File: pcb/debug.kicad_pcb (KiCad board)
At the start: 4 copper layers, 50 x 100 mm, 78 parts, among them J1 09032967825, J2 USB_C_Receptacle_USB2.0, J3 Conn_01x06_Female, Q1 Q_PNP_BCE, SW1 SW_DIP_x02, SW2 Reset, U1 STLQ020PU33R, U2 FT4222HQ, U3 STM32F103V8Tx, U4 INA381AxDSG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

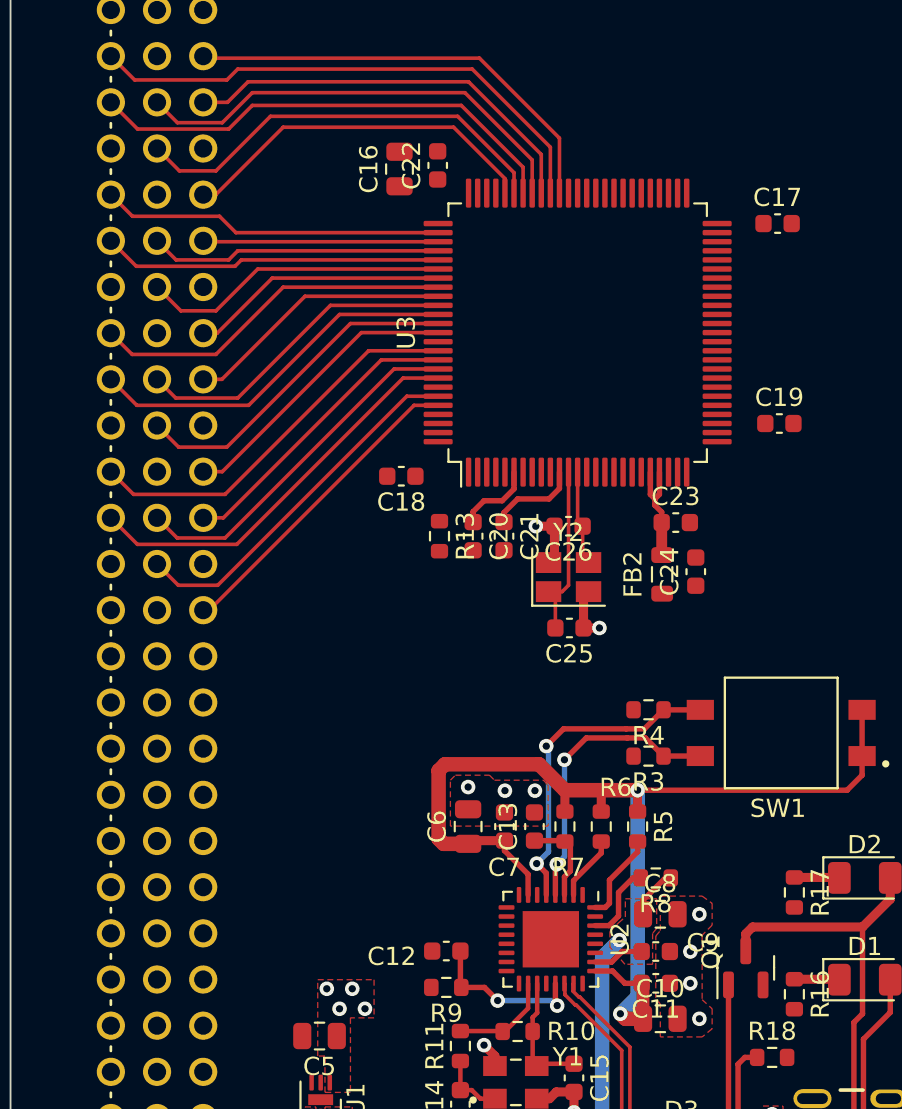
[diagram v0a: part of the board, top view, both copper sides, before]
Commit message: route more data traces
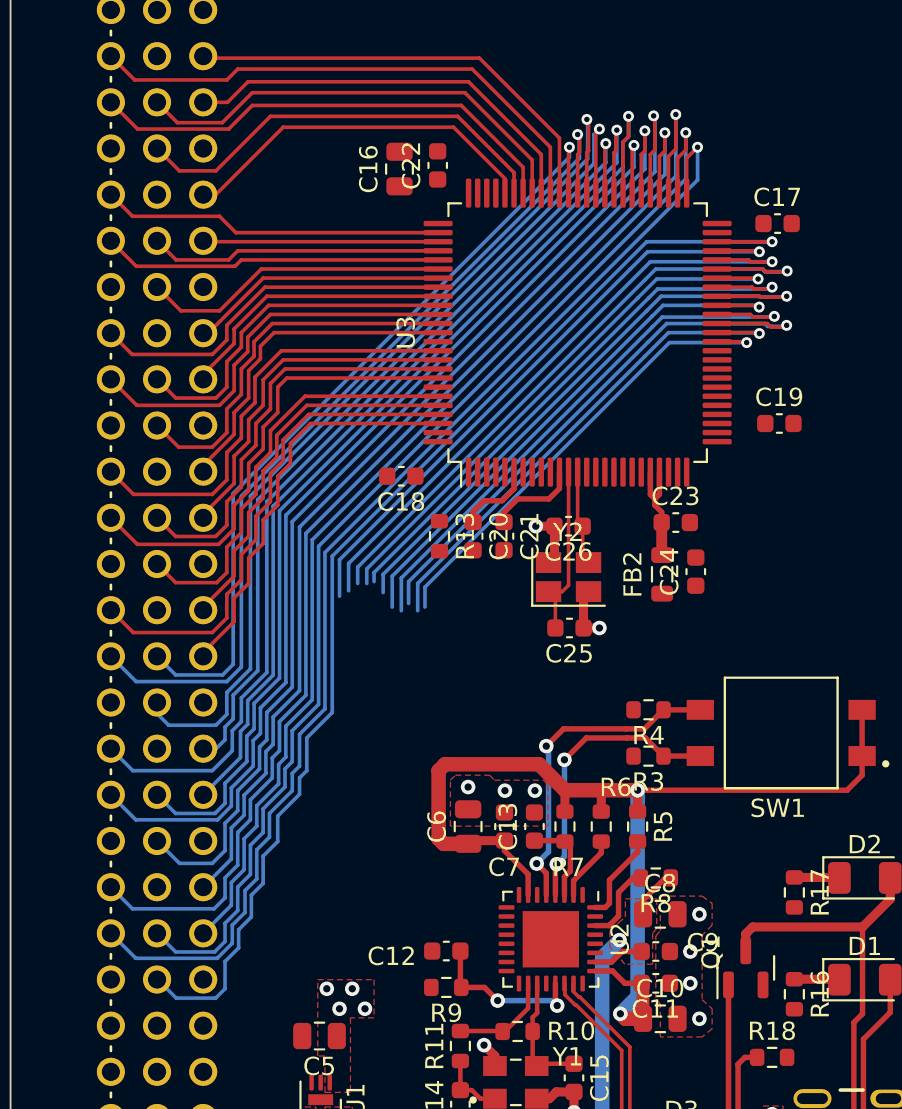
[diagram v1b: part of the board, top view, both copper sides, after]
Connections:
- U3 pad 37: unconnected-(U3-Pad37) -> CONN_0
- U3 pad 38: unconnected-(U3-Pad38) -> CONN_1
- U3 pad 39: unconnected-(U3-Pad39) -> CONN_2
- U3 pad 40: unconnected-(U3-Pad40) -> CONN_3
- U3 pad 41: unconnected-(U3-Pad41) -> CONN_4
- U3 pad 42: unconnected-(U3-Pad42) -> CONN_5
- U3 pad 43: unconnected-(U3-Pad43) -> CONN_6
- U3 pad 44: unconnected-(U3-Pad44) -> CONN_7
- U3 pad 45: unconnected-(U3-Pad45) -> CONN_8
- U3 pad 46: unconnected-(U3-Pad46) -> CONN_9
- U3 pad 47: unconnected-(U3-Pad47) -> CONN_10
- U3 pad 48: unconnected-(U3-Pad48) -> CONN_11
- U3 pad 51: unconnected-(U3-Pad51) -> CONN_12
- U3 pad 52: unconnected-(U3-Pad52) -> CONN_13
- U3 pad 53: unconnected-(U3-Pad53) -> CONN_14
- U3 pad 54: unconnected-(U3-Pad54) -> CONN_15
- U3 pad 55: unconnected-(U3-Pad55) -> CONN_16
- U3 pad 56: unconnected-(U3-Pad56) -> CONN_17
- U3 pad 57: unconnected-(U3-Pad57) -> CONN_18
- U3 pad 58: unconnected-(U3-Pad58) -> CONN_19
- U3 pad 59: unconnected-(U3-Pad59) -> CONN_20
- U3 pad 60: unconnected-(U3-Pad60) -> CONN_21
- U3 pad 61: unconnected-(U3-Pad61) -> CONN_22
- U3 pad 62: unconnected-(U3-Pad62) -> CONN_23
- U3 pad 63: unconnected-(U3-Pad63) -> CONN_24
- U3 pad 64: unconnected-(U3-Pad64) -> CONN_25
- U3 pad 86: unconnected-(U3-Pad86) -> CONN_36
- U3 pad 87: unconnected-(U3-Pad87) -> CONN_35
- U3 pad 88: unconnected-(U3-Pad88) -> CONN_34
- U3 pad 90: unconnected-(U3-Pad90) -> CONN_33
- U3 pad 91: unconnected-(U3-Pad91) -> CONN_32
- U3 pad 92: unconnected-(U3-Pad92) -> CONN_31
- U3 pad 93: unconnected-(U3-Pad93) -> CONN_30
- U3 pad 95: unconnected-(U3-Pad95) -> CONN_29
- U3 pad 96: unconnected-(U3-Pad96) -> CONN_28
- U3 pad 97: unconnected-(U3-Pad97) -> CONN_27
- U3 pad 98: unconnected-(U3-Pad98) -> CONN_26
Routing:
- net CONN_11: track 0.00 -> 65.0 mm, vias 0 -> 1
- net CONN_12: track 0.00 -> 64.8 mm, vias 0 -> 1
- net CONN_13: track 0.00 -> 62.9 mm, vias 0 -> 1
- net CONN_15: track 0.00 -> 62.6 mm, vias 0 -> 1
- net CONN_14: track 0.00 -> 60.3 mm, vias 0 -> 1
- net CONN_17: track 0.00 -> 57.2 mm, vias 0 -> 1
- net CONN_16: track 0.00 -> 57.1 mm, vias 0 -> 1
- net CONN_19: track 0.00 -> 55.7 mm, vias 0 -> 1
- net CONN_18: track 0.00 -> 55.7 mm, vias 0 -> 1
- net CONN_21: track 0.00 -> 52.3 mm, vias 0 -> 1
- net CONN_23: track 0.00 -> 50.1 mm, vias 0 -> 1
- net CONN_20: track 0.00 -> 49.5 mm, vias 0 -> 1
- net CONN_24: track 0.00 -> 48.4 mm, vias 0 -> 1
- net CONN_22: track 0.00 -> 47.1 mm, vias 0 -> 1
- net CONN_25: track 0.00 -> 43.5 mm, vias 0 -> 1
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
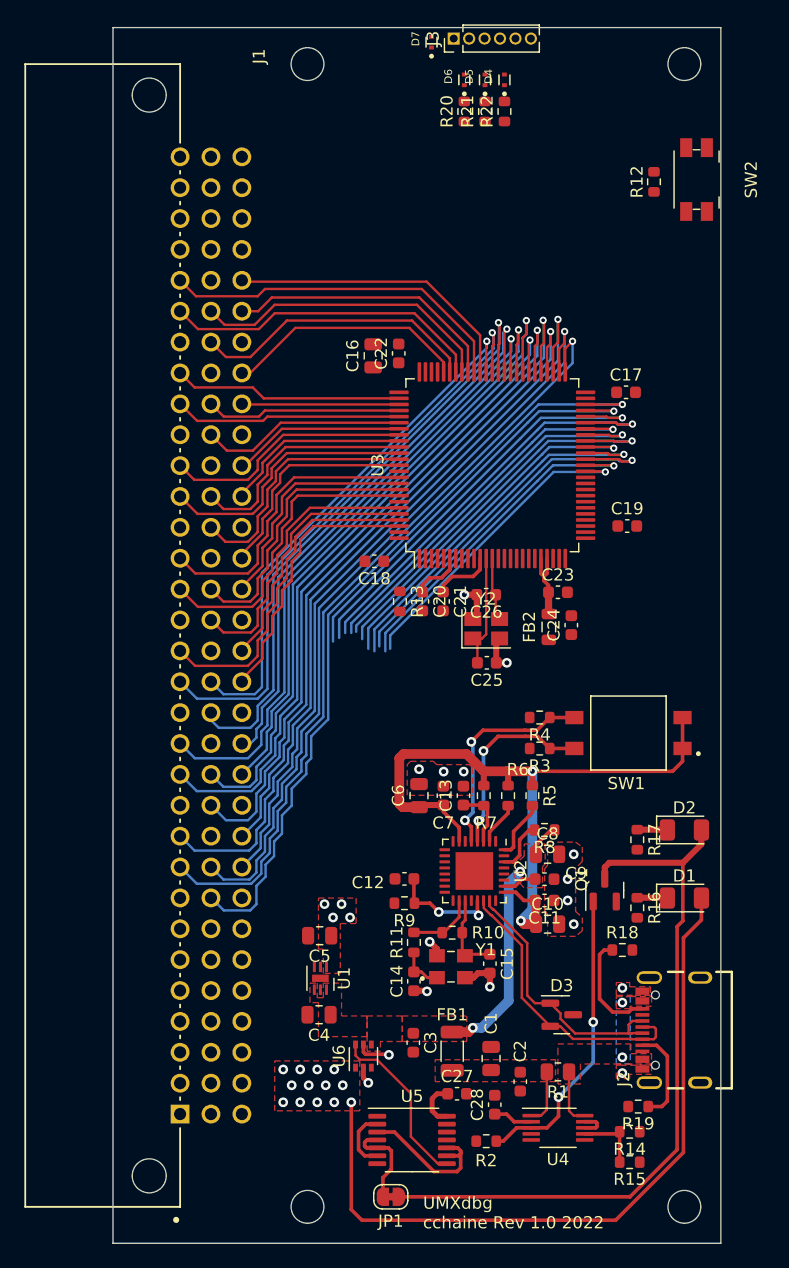
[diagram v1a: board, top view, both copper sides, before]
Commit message: finished routing the bus traces
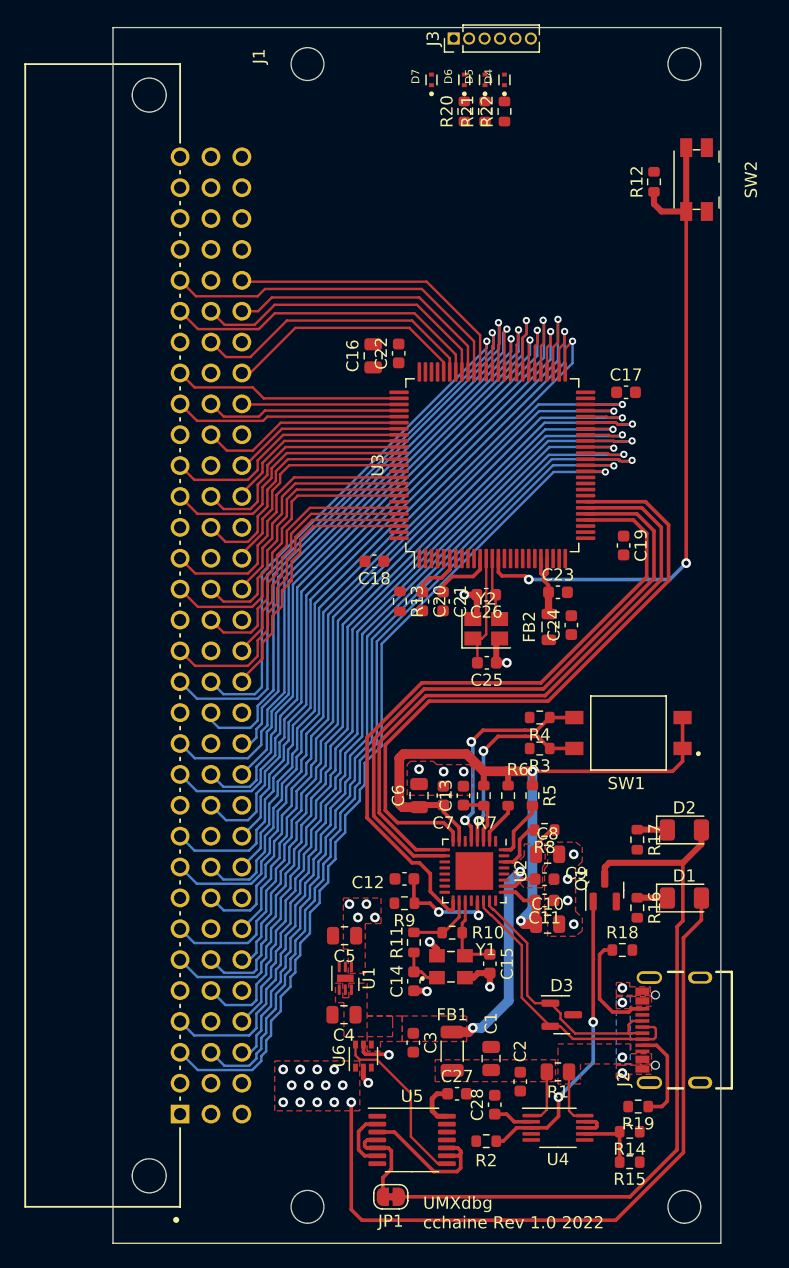
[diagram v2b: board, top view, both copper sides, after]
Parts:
- moved D7 3.10 mm to (105.2, 53.3)
- moved C4 2.05 mm to (98.0, 130.2)
- moved C5 2.05 mm to (98.0, 123.7)
- moved U1 2.05 mm to (98.1, 127.2)
- moved C19 1.63 mm to (121.0, 91.6), turned to -90 degrees
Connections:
- U3 pad 30: SPI_SCK -> SPI_MOSI
- U3 pad 32: SPI_MOSI -> SPI_SCK
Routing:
- net SPI_CS: track 0.00 -> 56.0 mm
- net RESET: track 0.00 -> 55.5 mm, vias 0 -> 2
- net SPI_SCK: track 0.00 -> 53.6 mm
- net SPI_MISO: track 0.00 -> 52.4 mm
- net SPI_MOSI: track 0.00 -> 52.1 mm
- net CONN_0: track 26.0 -> 71.9 mm
- net CONN_1: track 28.4 -> 70.7 mm
- net CONN_3: track 31.5 -> 73.5 mm
- net CONN_6: track 32.0 -> 70.7 mm
- net CONN_2: track 31.9 -> 70.4 mm
- net CONN_5: track 33.4 -> 71.1 mm
- net CONN_7: track 31.2 -> 66.4 mm
- net CONN_4: track 30.5 -> 65.4 mm
- net CONN_9: track 34.7 -> 69.0 mm
- net CONN_8: track 35.3 -> 66.1 mm
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
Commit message: add power vias
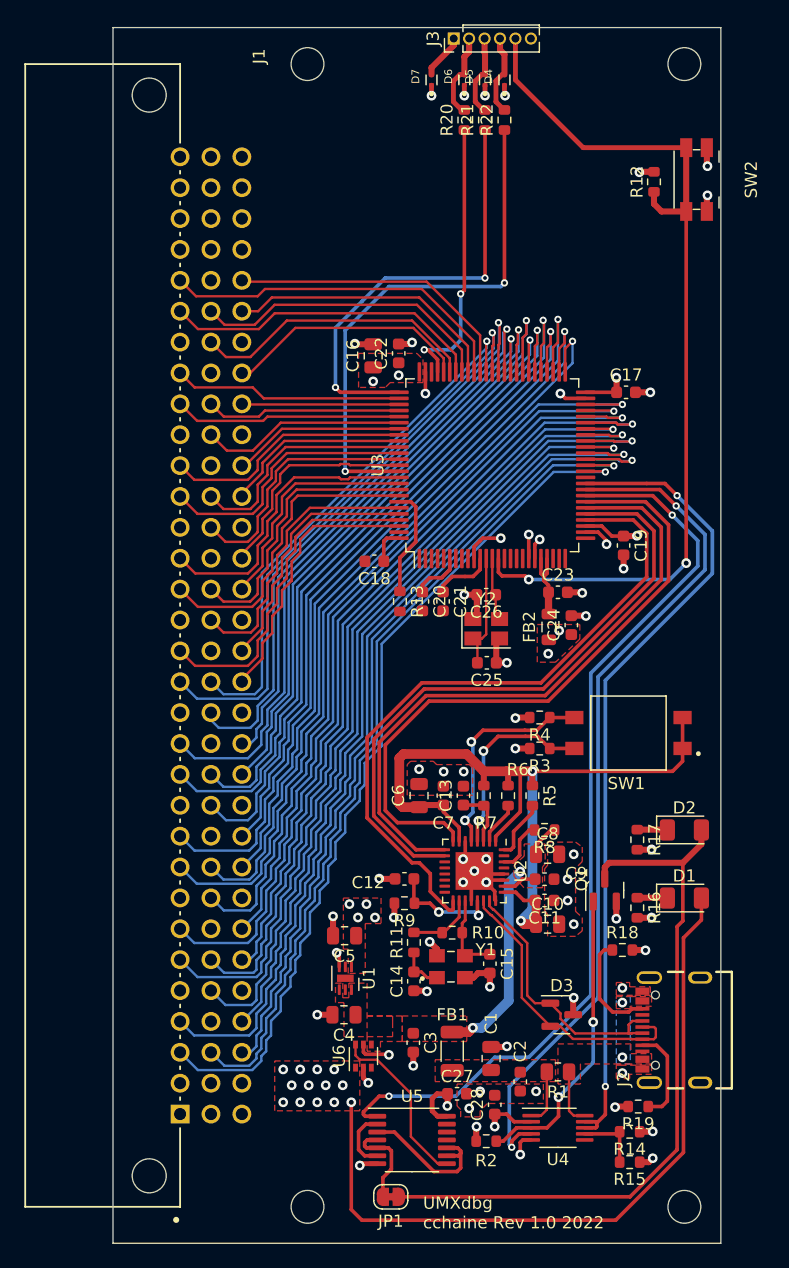
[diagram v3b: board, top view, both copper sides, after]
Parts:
- moved R20 0.70 mm to (107.9, 56.6)
- moved R21 0.70 mm to (109.6, 56.6)
- moved R22 0.70 mm to (111.2, 56.6)
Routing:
- net MODULE_ENABLE: track 0.00 -> 75.9 mm, vias 0 -> 2
- net MODULE_RESET: track 0.00 -> 70.9 mm, vias 0 -> 2
- net CURRENT_SENSE: track 2.38 -> 67.1 mm, vias 0 -> 2
- net GND: track 18.6 -> 80.9 mm, vias 16 -> 59
- net /MCU/MCU_SWTRACE: track 0.00 -> 43.3 mm, vias 0 -> 2
- net /MCU/MCU_SWCLK: track 0.00 -> 36.5 mm, vias 0 -> 2
- net /MCU/MCU_SWDIO: track 0.00 -> 23.2 mm, vias 0 -> 2
- net +3V3: track 16.4 -> 38.4 mm, vias 4 -> 16
- net RESET: track 55.5 -> 75.2 mm
- net /MCU/BOOT0: track 0.00 -> 9.05 mm
- net /MCU/SWDIO: track 0.00 -> 7.13 mm
- net /MCU/SWCLK: track 0.00 -> 6.78 mm
- net /MCU/SWTRACE: track 0.00 -> 6.73 mm
- net /VCCIO: track 61.6 -> 68.2 mm

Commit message: routed everything, need to add TP
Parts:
- moved R13 20.9 mm to (94.7, 76.9), turned to 90 degrees
- moved C18 3.45 mm to (101.5, 96.2), turned to -90 degrees
- moved C20 0.90 mm to (103.5, 96.2)
- moved C21 0.90 mm to (105.2, 96.2)
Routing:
- net GND: track 80.9 -> 93.9 mm, vias 59 -> 64
- net /MCU/BOOT0: track 9.05 -> 18.9 mm, vias 0 -> 2
- net +3V3: track 38.4 -> 45.4 mm, vias 16 -> 19

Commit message: finished pcb
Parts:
- removed SW1: SW_DIP_x02, DS04-254-2-02BK-SMT:SW_DS04-254-2-02BK-SMT
- added JP2: Jumper_2_Open, Jumper:SolderJumper-2_P1.3mm_Open_RoundedPad1.0x1.5mm, F.Cu at (122.3, 108.4)
- added JP3: Jumper_2_Open, Jumper:SolderJumper-2_P1.3mm_Open_RoundedPad1.0x1.5mm, F.Cu at (122.3, 105.6)
- added REF**: ESD-Logo_8.9x8mm_SilkScreen, Symbol:ESD-Logo_8.9x8mm_SilkScreen, F.Cu at (96.8, 100.8)
- added REF**: Symbol_GNU-Logo_SilkscreenTop, Symbol:Symbol_GNU-Logo_SilkscreenTop, F.Cu at (110.6, 65.8)
- added REF**: WEEE-Logo_5.6x8mm_SilkScreen, Symbol:WEEE-Logo_5.6x8mm_SilkScreen, F.Cu at (97.0, 112.6)
- added TP1: TestPoint_Small, TestPoint:TestPoint_Loop_D2.54mm_Drill1.5mm_Beaded, F.Cu at (95.2, 65.1)
- added TP2: TestPoint_Small, TestPoint:TestPoint_Loop_D2.54mm_Drill1.5mm_Beaded, F.Cu at (95.2, 59.6)
- added TP3: TestPoint_Small, TestPoint:TestPoint_Loop_D2.54mm_Drill1.5mm_Beaded, F.Cu at (123.2, 72.9)
- added TP4: TestPoint_Small, TestPoint:TestPoint_Loop_D2.54mm_Drill1.5mm_Beaded, F.Cu at (117.3, 143.9)
- added TP5: TestPoint_Small, TestPoint:TestPoint_Loop_D2.54mm_Drill1.5mm_Beaded, F.Cu at (118.6, 66.1)
- moved D4 3.20 mm to (108.0, 53.3)
- moved D6 3.20 mm to (104.7, 53.3)
- moved D7 3.20 mm to (102.0, 53.3)
- moved J3 3.20 mm to (103.8, 49.9)
- moved R20 3.20 mm to (104.7, 56.6)
- moved R22 3.20 mm to (108.0, 56.6)
- moved D5 3.20 mm to (106.4, 53.3)
- moved R21 3.20 mm to (106.4, 56.6)
- moved R12 1.20 mm to (122.3, 61.7)
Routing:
- net CURRENT_SENSE: track 67.1 -> 82.6 mm
- net +5V_Mod: track 60.4 -> 66.9 mm
- net VBUS: track 4.66 -> 10.7 mm
- net RESET: track 75.2 -> 80.9 mm
- net /DCNF1: track 18.0 -> 22.8 mm
- net /DCNF0: track 16.0 -> 20.8 mm
- net /MCU/MCU_SWTRACE: track 43.3 -> 38.9 mm
- net /MCU/MCU_SWCLK: track 36.5 -> 32.0 mm
- net /VCCIO: track 68.2 -> 65.4 mm
- net /MCU/MCU_SWDIO: track 23.2 -> 20.6 mm
- net Net-(D2-A): track 59.2 -> 60.2 mm
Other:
- board text added: "+3v3"
- board text added: "+5V_Mod"
- board text added: "CURRENT SENSE"
- board text added: "DCNF0"
- board text added: "DCNF1"
- board text added: "GND"
- board text added: "Module powered"
- board text added: "Overcurrent"
- board text added: "RESET"
- board text added: "SWCLK"
- board text added: "SWDIO"
- board text added: "SWTRACE"
- board text added: "VBUS"
